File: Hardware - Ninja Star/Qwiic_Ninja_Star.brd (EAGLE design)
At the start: 40.6 x 40.6 mm, 18 parts, among them J1 QWIIC_RIGHT_ANGLE, J2 QWIIC_RIGHT_ANGLE, J3 QWIIC_RIGHT_ANGLE, J4 QWIIC_RIGHT_ANGLE

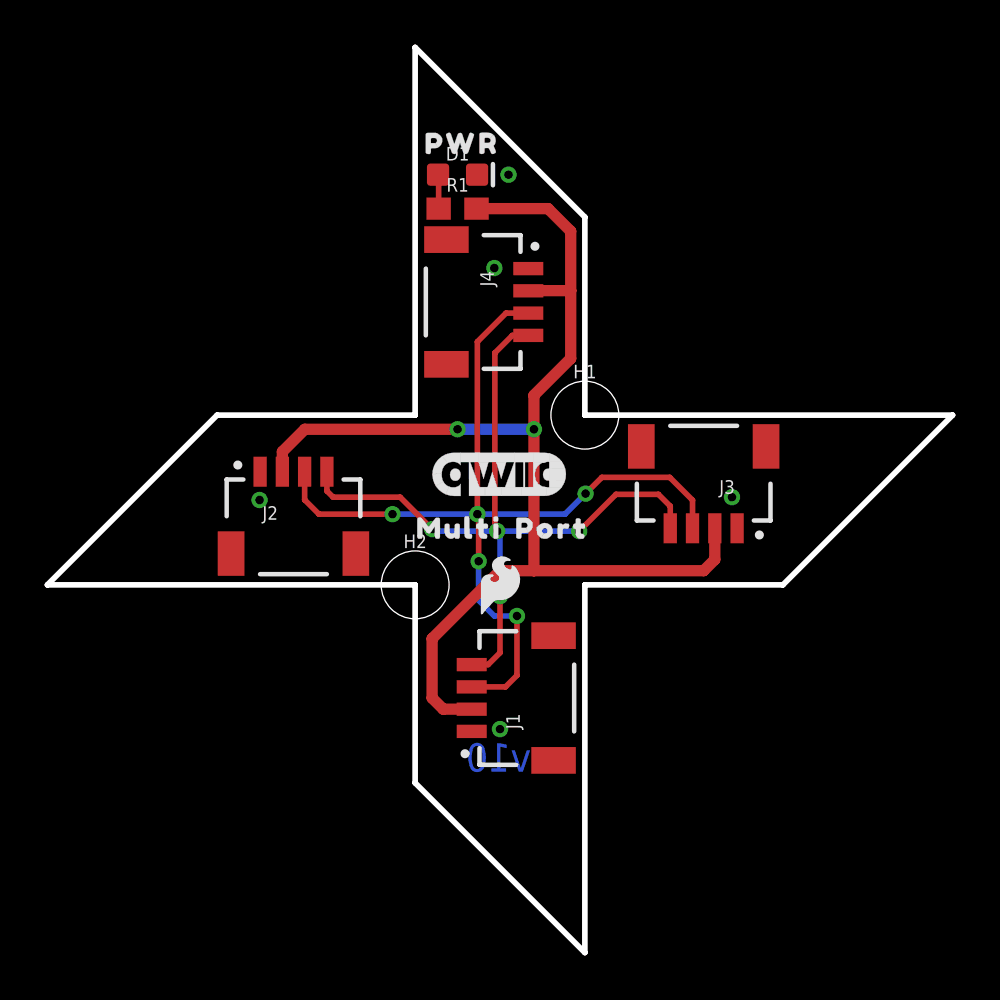
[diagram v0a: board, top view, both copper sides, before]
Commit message: Ninja Star: Design Review Changes
Added jumper to PWR LED
Added fiducials
Added OSHW, qwiic, SF, and flame logo devices to schematic
Tried my best to move traces out from underneath screws
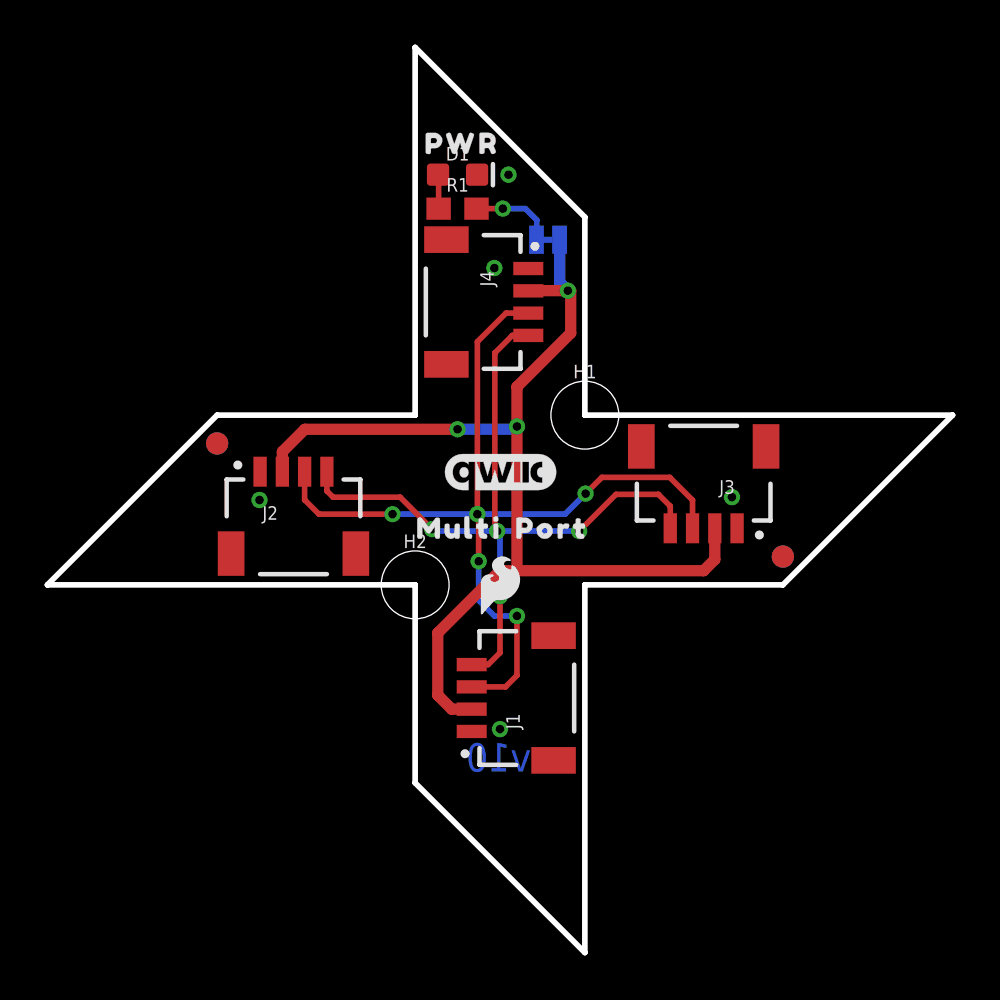
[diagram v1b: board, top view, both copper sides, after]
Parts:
- removed U$3: (no value), SparkFun-Aesthetics:QWIIC_6MM
- added FD1, FD2, FD3, FD4: FIDUCIAL1X2, SparkFun-Aesthetics:FIDUCIAL-1X2
- added JP1: PWR_LED, SparkFun-Jumpers:SMT-JUMPER_2_NC_TRACE_SILK
- added LOGO1, LOGO2: QWIIC_LOGO_5MM, SparkFun-Aesthetics:QWIIC_5MM
- added LOGO3: OSHW-LOGOS, SparkFun-Aesthetics:OSHW-LOGO-S
- added LOGO5, LOGO6, LOGO7, LOGO8: SFE_LOGO_FLAME.1_INCH, SparkFun-Aesthetics:SFE_LOGO_FLAME_.1
- added U$4: (no value), output:PWR0
- LOGO4: value (none) -> SFE_LOGO_NAME.2_INCH
- U$1: device SparkFun-Aesthetics:QWIIC_6MM -> SparkFun-Aesthetics:ORDERING_INSTRUCTIONS
- moved U$1 38.0 mm to (44.5, 50.8)
- renumbered U$6 to LOGO4
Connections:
- new net N$2: JP1.1, R1.2
- net 3.3V: now also JP1.2; no longer R1.2
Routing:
- net 3.3V: track 55.3 -> 49.6 mm, vias 2 -> 3
- net N$2: track 0.00 -> 3.81 mm, vias 0 -> 1
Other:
- board text added: "0.8mm board"
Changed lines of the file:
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@@
 <layer number="37" name="tTest" color="7" fill="1" visible="no" active="yes"/>
 <layer number="38" name="bTest" color="7" fill="1" visible="no" active="yes"/>
-<layer number="39" name="tKeepout" color="4" fill="11" visible="no" active="yes"/>
+<layer number="39" name="tKeepout" color="4" fill="11" visible="yes" active="yes"/>
 <layer number="40" name="bKeepout" color="1" fill="11" visible="no" active="yes"/>
-<layer number="41" name="tRestrict" color="4" fill="10" visible="no" active="yes"/>
+<layer number="41" name="tRestrict" color="4" fill="10" visible="yes" active="yes"/>
 <layer number="42" name="bRestrict" color="1" fill="10" visible="no" active="yes"/>
 <layer number="43" name="vRestrict" color="2" fill="10" visible="no" active="yes"/>
@@
 <wire x1="24.13" y1="0" x2="16.51" y2="7.62" width="0.254" layer="20"/>
 <wire x1="0" y1="16.51" x2="7.62" y2="24.13" width="0.254" layer="20"/>
+<text x="45.72" y="38.1" size="1.27" layer="51" font="vector" ratio="15">0.8mm board</text>
 </plain>
 <attributes>
@@
 <attribute name="VALUE" x="18.288" y="30.861" size="0.6096" layer="27" font="vector" ratio="20" rot="R270"/>
 </element>
-<element name="U$1" library="SparkFun-Aesthetics" package="QWIIC_6MM" value="" x="20.32" y="21.463" smashed="yes"/>
-<element name="U$3" library="SparkFun-Aesthetics" package="QWIIC_6MM" value="" x="20.32" y="13.843" smashed="yes" rot="MR0"/>
 <element name="H1" library="SparkFun-Hardware" package="STAND-OFF-TIGHT" value="STAND-OFFTIGHT" x="24.13" y="24.13" smashed="yes">
 <attribute name="NAME" x="24.13" y="25.781" size="0.6096" layer="25" font="vector" ratio="20" align="bottom-center"/>
@@
 </element>
 <element name="U$2" library="SparkFun-Aesthetics" package="SFE_LOGO_FLAME_.1" value="" x="20.32" y="16.51" smashed="yes"/>
-<element name="U$6" library="SparkFun-Aesthetics" package="SFE_LOGO_NAME_.2" value="" x="20.32" y="20.32" smashed="yes" rot="MR0"/>
 <element name="U$9" library="output" package="PWR0" value="" x="16.256" y="36.322" smashed="yes"/>
 <element name="U$10" library="output" package="MULTI0" value="" x="15.875" y="19.05" smashed="yes"/>
@@
 <element name="U$12" library="output" package="PORT0" value="" x="20.32" y="19.05" smashed="yes"/>
 <element name="U$13" library="output" package="PORT0" value="" x="22.606" y="10.414" smashed="yes" rot="MR0"/>
+<element name="JP1" library="SparkFun-Jumpers" package="SMT-JUMPER_2_NC_TRACE_SILK" package3d_urn="urn:adsk.eagle:package:39281/1" value="PWR_LED" x="22.479" y="32.004" smashed="yes" rot="MR180">
+<attribute name="NAME" x="22.479" y="30.861" size="0.6096" layer="26" font="vector" ratio="20" rot="MR180" align="bottom-center"/>
+<attribute name="VALUE" x="22.479" y="33.147" size="0.6096" layer="28" font="vector" ratio="20" rot="MR180" align="top-center"/>
+</element>
+<element name="FD1" library="SparkFun-Aesthetics" package="FIDUCIAL-1X2" value="FIDUCIAL1X2" x="7.62" y="22.86" smashed="yes"/>
+<element name="FD2" library="SparkFun-Aesthetics" package="FIDUCIAL-1X2" value="FIDUCIAL1X2" x="7.62" y="22.86" smashed="yes" rot="MR0"/>
+<element name="FD3" library="SparkFun-Aesthetics" package="FIDUCIAL-1X2" value="FIDUCIAL1X2" x="33.02" y="17.78" smashed="yes"/>
+<element name="FD4" library="SparkFun-Aesthetics" package="FIDUCIAL-1X2" value="FIDUCIAL1X2" x="33.02" y="17.78" smashed="yes" rot="MR0"/>
+<element name="LOGO1" library="SparkFun-Aesthetics" package="QWIIC_5MM" value="QWIIC_LOGO_5MM" x="20.32" y="13.97" smashed="yes" rot="MR0"/>
+<element name="LOGO2" library="SparkFun-Aesthetics" package="QWIIC_5MM" value="QWIIC_LOGO_5MM" x="20.32" y="21.59" smashed="yes"/>
+<element name="LOGO3" library="SparkFun-Aesthetics" package="OSHW-LOGO-S" value="OSHW-LOGOS" x="20.32" y="25.4" smashed="yes" rot="MR0"/>
+<element name="LOGO4" library="SparkFun-Aesthetics" package="SFE_LOGO_NAME_.2" value="SFE_LOGO_NAME.2_INCH" x="20.32" y="20.32" smashed="yes" rot="MR0"/>
+<element name="U$4" library="output" package="PWR0" value="" x="21.336" y="32.004" smashed="yes" rot="MR0"/>
+<element name="LOGO5" library="SparkFun-Aesthetics" package="SFE_LOGO_FLAME_.1" value="SFE_LOGO_FLAME.1_INCH" x="37.465" y="22.733" smashed="yes" rot="MR270"/>
+<element name="LOGO6" library="SparkFun-Aesthetics" package="SFE_LOGO_FLAME_.1" value="SFE_LOGO_FLAME.1_INCH" x="17.907" y="37.592" smashed="yes" rot="MR180"/>
+<element name="LOGO7" library="SparkFun-Aesthetics" package="SFE_LOGO_FLAME_.1" value="SFE_LOGO_FLAME.1_INCH" x="22.606" y="3.302" smashed="yes" rot="MR0"/>
+<element name="LOGO8" library="SparkFun-Aesthetics" package="SFE_LOGO_FLAME_.1" value="SFE_LOGO_FLAME.1_INCH" x="3.429" y="18.161" smashed="yes" rot="MR90"/>
+<element name="U$1" library="SparkFun-Aesthetics" package="ORDERING_INSTRUCTIONS" value="" x="44.45" y="50.8" smashed="yes"/>
 </elements>
 <signals>
@@
 <contactref element="J2" pad="2"/>
 <contactref element="J4" pad="2"/>
-<contactref element="R1" pad="2"/>
 <wire x1="21.59" y1="29.71" x2="21.598" y2="29.718" width="0.508" layer="1"/>
-<wire x1="21.598" y1="29.718" x2="23.495" y2="29.718" width="0.508" layer="1"/>
-<wire x1="21.844" y1="25.019" x2="23.495" y2="26.67" width="0.508" layer="1"/>
-<wire x1="21.844" y1="25.019" x2="21.844" y2="23.495" width="0.508" layer="1"/>
-<wire x1="21.844" y1="23.495" x2="21.844" y2="17.145" width="0.508" layer="1"/>
+<wire x1="21.598" y1="29.718" x2="23.368" y2="29.718" width="0.508" layer="1"/>
+<wire x1="23.368" y1="29.718" x2="23.495" y2="29.718" width="0.508" layer="1"/>
+<wire x1="21.082" y1="25.4" x2="23.495" y2="27.813" width="0.508" layer="1"/>
+<wire x1="21.082" y1="25.4" x2="21.082" y2="23.622" width="0.508" layer="1"/>
+<wire x1="21.082" y1="23.622" x2="21.082" y2="17.145" width="0.508" layer="1"/>
 <wire x1="29.964" y1="19.05" x2="29.964" y2="17.645" width="0.508" layer="1"/>
 <wire x1="29.964" y1="17.645" x2="29.464" y2="17.145" width="0.508" layer="1"/>
-<wire x1="29.464" y1="17.145" x2="21.844" y2="17.145" width="0.508" layer="1"/>
-<wire x1="19.05" y1="10.93" x2="17.772" y2="10.93" width="0.508" layer="1"/>
-<wire x1="17.772" y1="10.93" x2="17.272" y2="11.43" width="0.508" layer="1"/>
-<wire x1="17.272" y1="14.095203125" x2="17.272" y2="11.43" width="0.508" layer="1"/>
-<wire x1="21.844" y1="17.145" x2="20.321796875" y2="17.145" width="0.508" layer="1"/>
-<wire x1="20.321796875" y1="17.145" x2="17.272" y2="14.095203125" width="0.508" layer="1"/>
+<wire x1="29.464" y1="17.145" x2="21.082" y2="17.145" width="0.508" layer="1"/>
+<wire x1="19.05" y1="10.93" x2="18.153" y2="10.93" width="0.508" layer="1"/>
+<wire x1="18.153" y1="10.93" x2="17.526" y2="11.557" width="0.508" layer="1"/>
+<wire x1="17.526" y1="14.349203125" x2="17.526" y2="11.557" width="0.508" layer="1"/>
+<wire x1="21.082" y1="17.145" x2="20.321796875" y2="17.145" width="0.508" layer="1"/>
+<wire x1="20.321796875" y1="17.145" x2="17.526" y2="14.349203125" width="0.508" layer="1"/>
 <wire x1="10.549" y1="21.59" x2="10.549" y2="22.487" width="0.508" layer="1"/>
 <wire x1="11.557" y1="23.495" x2="18.415" y2="23.495" width="0.508" layer="1"/>
 <via x="18.415" y="23.495" extent="1-16" drill="0.381"/>
-<wire x1="21.844" y1="23.495" x2="18.415" y2="23.495" width="0.508" layer="16"/>
-<via x="21.844" y="23.495" extent="1-16" drill="0.381"/>
+<wire x1="21.082" y1="23.622" x2="20.955" y2="23.495" width="0.508" layer="16"/>
+<wire x1="20.955" y1="23.495" x2="18.415" y2="23.495" width="0.508" layer="16"/>
+<via x="21.082" y="23.622" extent="1-16" drill="0.381"/>
 <wire x1="10.549" y1="22.487" x2="11.557" y2="23.495" width="0.508" layer="1"/>
-<wire x1="19.265" y1="33.401" x2="22.479" y2="33.401" width="0.508" layer="1"/>
-<wire x1="23.495" y1="32.385" x2="23.495" y2="29.718" width="0.508" layer="1"/>
-<wire x1="22.479" y1="33.401" x2="23.495" y2="32.385" width="0.508" layer="1"/>
-<wire x1="23.495" y1="26.67" x2="23.495" y2="29.718" width="0.508" layer="1"/>
+<wire x1="23.495" y1="27.813" x2="23.495" y2="29.718" width="0.508" layer="1"/>
+<contactref element="JP1" pad="2"/>
+<wire x1="22.9997" y1="32.004" x2="22.9997" y2="30.0863" width="0.508" layer="16"/>
+<wire x1="22.9997" y1="30.0863" x2="23.368" y2="29.718" width="0.508" layer="16"/>
+<via x="23.368" y="29.718" extent="1-16" drill="0.381"/>
 </signal>
 <signal name="N$1">
@@
 <wire x1="17.565" y1="33.401" x2="17.565" y2="34.898" width="0.254" layer="1"/>
 <wire x1="17.565" y1="34.898" x2="17.538" y2="34.925" width="0.254" layer="1"/>
+</signal>
+<signal name="N$2">
+<contactref element="JP1" pad="1"/>
+<contactref element="R1" pad="2"/>
+<wire x1="19.265" y1="33.401" x2="20.447" y2="33.401" width="0.254" layer="1"/>
+<via x="20.447" y="33.401" extent="1-16" drill="0.381"/>
+<wire x1="20.447" y1="33.401" x2="21.463" y2="33.401" width="0.254" layer="16"/>
+<wire x1="21.463" y1="33.401" x2="21.971" y2="32.893" width="0.254" layer="16"/>
+<wire x1="21.971" y1="32.893" x2="21.971" y2="32.0167" width="0.254" layer="16"/>
+<wire x1="21.971" y1="32.0167" x2="21.9583" y2="32.004" width="0.254" layer="16"/>
 </signal>
 </signals>
@@
 </board>
 </drawing>
+<compatibility>
+<note version="8.3" severity="warning">
+Since Version 8.3, EAGLE supports URNs for individual library
+assets (packages, symbols, and devices). The URNs of those assets
+will not be understood (or retained) with this version.
+</note>
+<note version="8.3" severity="warning">
+Since Version 8.3, EAGLE supports the association of 3D packages
+with devices in libraries, schematics, and board files. Those 3D
+packages will not be understood (or retained) with this version.
+</note>
+</compatibility>
 </eagle>

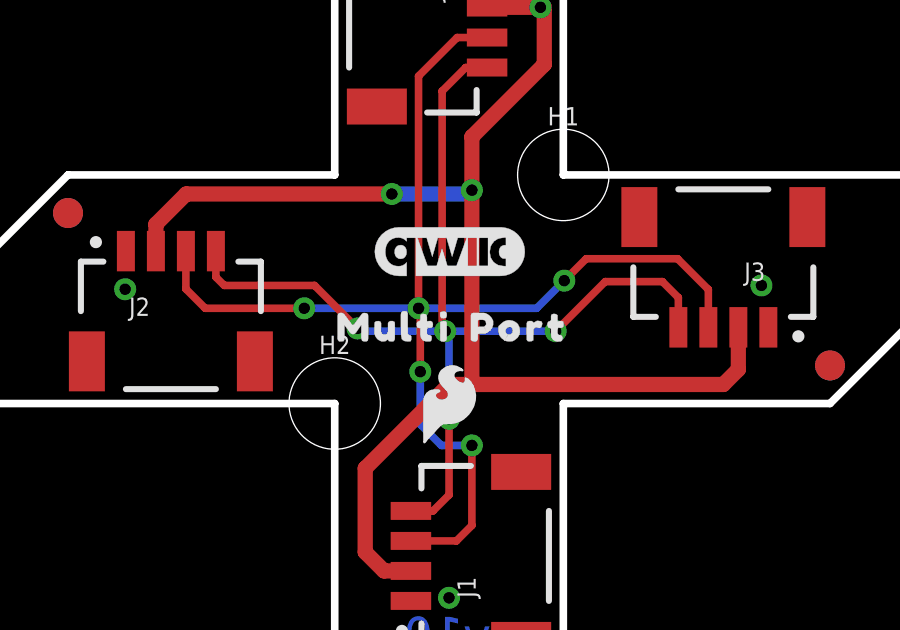
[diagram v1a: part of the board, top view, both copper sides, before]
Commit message: Update silkscreen name to "Ninja Star"
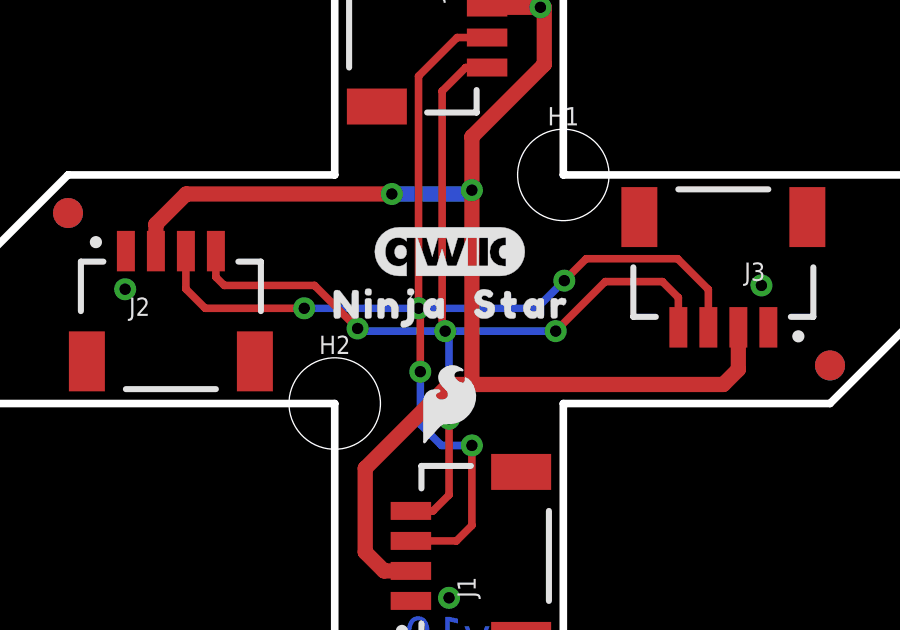
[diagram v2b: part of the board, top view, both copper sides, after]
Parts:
- removed U$10, U$11: (no value), output:MULTI0
- removed U$12, U$13: (no value), output:PORT0
- added U$3, U$5: (no value), output:NINJA0
- added U$6, U$7: (no value), output:STAR0
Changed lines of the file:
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@@
 <?xml version="1.0" encoding="utf-8"?>
 <!DOCTYPE eagle SYSTEM "eagle.dtd">
-<eagle version="9.5.2">
+<eagle version="9.6.2">
 <drawing>
 <settings>
@@
 <element name="U$2" library="SparkFun-Aesthetics" package="SFE_LOGO_FLAME_.1" value="" x="20.32" y="16.51" smashed="yes"/>
 <element name="U$9" library="output" package="PWR0" value="" x="16.256" y="36.322" smashed="yes"/>
-<element name="U$10" library="output" package="MULTI0" value="" x="15.875" y="19.05" smashed="yes"/>
-<element name="U$11" library="output" package="MULTI0" value="" x="22.86" y="11.811" smashed="yes" rot="MR0"/>
-<element name="U$12" library="output" package="PORT0" value="" x="20.32" y="19.05" smashed="yes"/>
-<element name="U$13" library="output" package="PORT0" value="" x="22.606" y="10.414" smashed="yes" rot="MR0"/>
 <element name="JP1" library="SparkFun-Jumpers" package="SMT-JUMPER_2_NC_TRACE_SILK" package3d_urn="urn:adsk.eagle:package:39281/1" value="PWR_LED" x="22.479" y="32.004" smashed="yes" rot="MR180">
 <attribute name="NAME" x="22.479" y="30.861" size="0.6096" layer="26" font="vector" ratio="20" rot="MR180" align="bottom-center"/>
@@
 <element name="LOGO8" library="SparkFun-Aesthetics" package="SFE_LOGO_FLAME_.1" value="SFE_LOGO_FLAME.1_INCH" x="3.429" y="18.161" smashed="yes" rot="MR90"/>
 <element name="U$1" library="SparkFun-Aesthetics" package="ORDERING_INSTRUCTIONS" value="" x="44.45" y="50.8" smashed="yes"/>
+<element name="U$3" library="output" package="NINJA0" value="" x="15.748" y="19.812" smashed="yes"/>
+<element name="U$5" library="output" package="NINJA0" value="" x="22.86" y="12.065" smashed="yes" rot="MR0"/>
+<element name="U$6" library="output" package="STAR0" value="" x="20.447" y="19.812" smashed="yes"/>
+<element name="U$7" library="output" package="STAR0" value="" x="22.479" y="10.668" smashed="yes" rot="MR0"/>
 </elements>
 <signals>

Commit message: Completed Engineering checklist
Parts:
- moved U$3 0.18 mm to (15.6, 19.7)
- moved U$6 0.13 mm to (20.4, 19.7)
- moved U$5 0.13 mm to (22.9, 12.2)
- moved U$7 0.13 mm to (22.5, 10.8)
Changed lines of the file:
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@@
 <?xml version="1.0" encoding="utf-8"?>
 <!DOCTYPE eagle SYSTEM "eagle.dtd">
-<eagle version="9.6.2">
+<eagle version="9.5.2">
 <drawing>
 <settings>
-<setting alwaysvectorfont="no"/>
+<setting alwaysvectorfont="yes"/>
 <setting verticaltext="up"/>
 </settings>
@@
 <layer number="37" name="tTest" color="7" fill="1" visible="no" active="yes"/>
 <layer number="38" name="bTest" color="7" fill="1" visible="no" active="yes"/>
-<layer number="39" name="tKeepout" color="4" fill="11" visible="yes" active="yes"/>
+<layer number="39" name="tKeepout" color="4" fill="11" visible="no" active="yes"/>
 <layer number="40" name="bKeepout" color="1" fill="11" visible="no" active="yes"/>
-<layer number="41" name="tRestrict" color="4" fill="10" visible="yes" active="yes"/>
+<layer number="41" name="tRestrict" color="4" fill="10" visible="no" active="yes"/>
 <layer number="42" name="bRestrict" color="1" fill="10" visible="no" active="yes"/>
 <layer number="43" name="vRestrict" color="2" fill="10" visible="no" active="yes"/>
@@
 <element name="LOGO8" library="SparkFun-Aesthetics" package="SFE_LOGO_FLAME_.1" value="SFE_LOGO_FLAME.1_INCH" x="3.429" y="18.161" smashed="yes" rot="MR90"/>
 <element name="U$1" library="SparkFun-Aesthetics" package="ORDERING_INSTRUCTIONS" value="" x="44.45" y="50.8" smashed="yes"/>
-<element name="U$3" library="output" package="NINJA0" value="" x="15.748" y="19.812" smashed="yes"/>
-<element name="U$5" library="output" package="NINJA0" value="" x="22.86" y="12.065" smashed="yes" rot="MR0"/>
-<element name="U$6" library="output" package="STAR0" value="" x="20.447" y="19.812" smashed="yes"/>
-<element name="U$7" library="output" package="STAR0" value="" x="22.479" y="10.668" smashed="yes" rot="MR0"/>
+<element name="U$3" library="output" package="NINJA0" value="" x="15.621" y="19.685" smashed="yes"/>
+<element name="U$5" library="output" package="NINJA0" value="" x="22.86" y="12.192" smashed="yes" rot="MR0"/>
+<element name="U$6" library="output" package="STAR0" value="" x="20.447" y="19.685" smashed="yes"/>
+<element name="U$7" library="output" package="STAR0" value="" x="22.479" y="10.795" smashed="yes" rot="MR0"/>
 </elements>
 <signals>
